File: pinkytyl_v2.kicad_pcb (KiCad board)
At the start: 2 copper layers, 132 x 105.9 mm, 66 parts, among them J1 50-00174, J2 Conn_01x02, J3 USB_B_Mini, J5 Conn_02x05_Odd_Even, K0 KEYSW, K10 KEYSW, K11 KEYSW, K12 KEYSW, K13 KEYSW, K14 KEYSW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

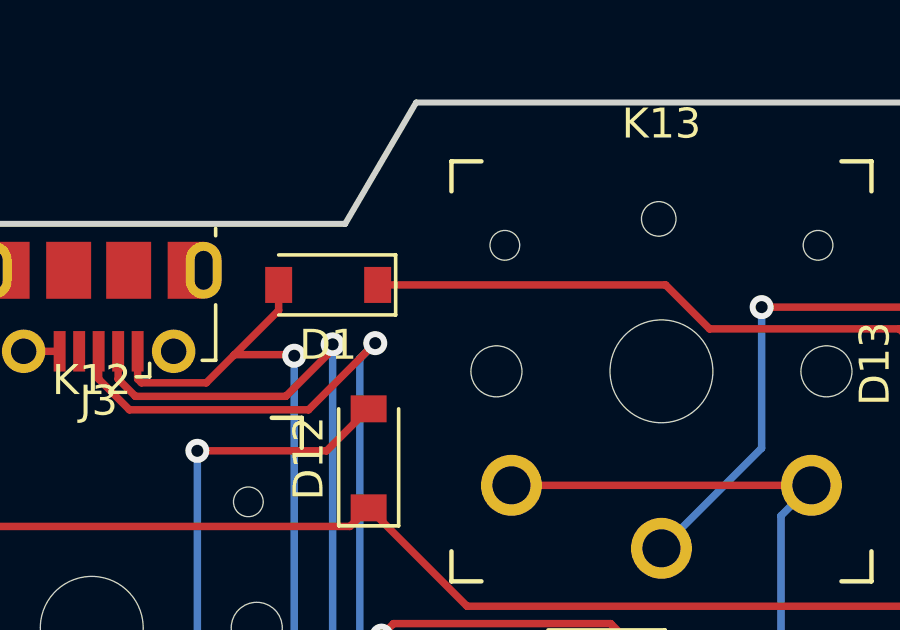
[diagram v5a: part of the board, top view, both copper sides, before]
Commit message: Changed my mind regarding detection of VUSB, software solution is doing fine with less components
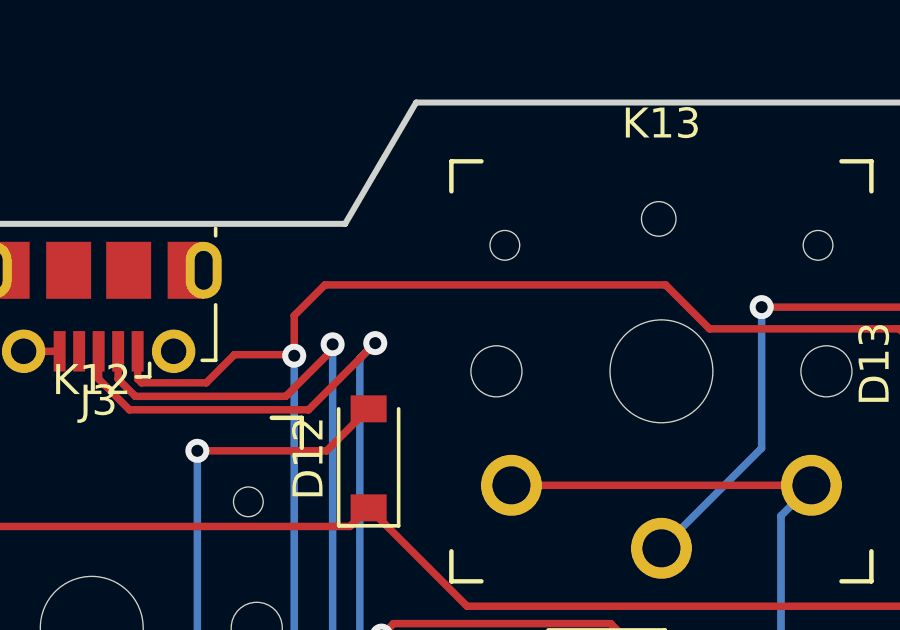
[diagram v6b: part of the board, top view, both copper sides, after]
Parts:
- removed D1: D, Diode_SMD:D_SOD-123
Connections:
- J3 pad 1: UVCC -> VCC
- U1 pad 7: UVCC -> VCC
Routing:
- net VCC: track 208.6 -> 326.3 mm, vias 7 -> 11
- net UVCC: track 116.1 -> 0.00 mm, vias 4 -> 0
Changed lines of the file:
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@@
     (tracks 594)
     (zones 0)
-    (modules 66)
-    (nets 64)
+    (modules 65)
+    (nets 63)
   )
   (page A4)
@@
   (net 61 "Net-(U1-Pad41)")
   (net 62 "Net-(D0-Pad2)")
-  (net 63 UVCC)
   (net_class Default "This is the default net class."
     (clearance 0.2)
@@
     (add_net "Net-(U1-Pad41)")
     (add_net "Net-(U1-Pad8)")
-    (add_net UVCC)
     (add_net VCC)
     (add_net c0)
@@
     (pad "" np_thru_hole circle (at -5.22 -4.2) (size 0.9906 0.9906) (drill 0.9906) (layers *.Cu *.Mask))
   )
-  (module Diode_SMD:D_SOD-123 (layer F.Cu)
-    (at 125.49 42.26 180)
-    (descr SOD-123)
-    (tags SOD-123)
-    (attr smd)
-    (fp_text reference D1 (at 0 -2) (layer F.SilkS)
-      (effects (font (size 1 1) (thickness 0.15)))
-    )
-    (fp_text value D (at 0 2.1) (layer F.Fab)
-      (effects (font (size 1 1) (thickness 0.15)))
-    )
-    (fp_text user %R (at 0 -2) (layer F.Fab)
-      (effects (font (size 1 1) (thickness 0.15)))
-    )
-    (fp_line (start -2.25 -1) (end -2.25 1) (layer F.SilkS) (width 0.12))
-    (fp_line (start 0.25 0) (end 0.75 0) (layer F.Fab) (width 0.1))
-    (fp_line (start 0.25 0.4) (end -0.35 0) (layer F.Fab) (width 0.1))
-    (fp_line (start 0.25 -0.4) (end 0.25 0.4) (layer F.Fab) (width 0.1))
-    (fp_line (start -0.35 0) (end 0.25 -0.4) (layer F.Fab) (width 0.1))
-    (fp_line (start -0.35 0) (end -0.35 0.55) (layer F.Fab) (width 0.1))
-    (fp_line (start -0.35 0) (end -0.35 -0.55) (layer F.Fab) (width 0.1))
-    (fp_line (start -0.75 0) (end -0.35 0) (layer F.Fab) (width 0.1))
-    (fp_line (start -1.4 0.9) (end -1.4 -0.9) (layer F.Fab) (width 0.1))
-    (fp_line (start 1.4 0.9) (end -1.4 0.9) (layer F.Fab) (width 0.1))
-    (fp_line (start 1.4 -0.9) (end 1.4 0.9) (layer F.Fab) (width 0.1))
-    (fp_line (start -1.4 -0.9) (end 1.4 -0.9) (layer F.Fab) (width 0.1))
-    (fp_line (start -2.35 -1.15) (end 2.35 -1.15) (layer F.CrtYd) (width 0.05))
-    (fp_line (start 2.35 -1.15) (end 2.35 1.15) (layer F.CrtYd) (width 0.05))
-    (fp_line (start 2.35 1.15) (end -2.35 1.15) (layer F.CrtYd) (width 0.05))
-    (fp_line (start -2.35 -1.15) (end -2.35 1.15) (layer F.CrtYd) (width 0.05))
-    (fp_line (start -2.25 1) (end 1.65 1) (layer F.SilkS) (width 0.12))
-    (fp_line (start -2.25 -1) (end 1.65 -1) (layer F.SilkS) (width 0.12))
-    (pad 2 smd rect (at 1.65 0 180) (size 0.9 1.2) (layers F.Cu F.Paste F.Mask)
-      (net 63 UVCC))
-    (pad 1 smd rect (at -1.65 0 180) (size 0.9 1.2) (layers F.Cu F.Paste F.Mask)
-      (net 1 VCC))
-    (model ${KISYS3DMOD}/Diode_SMD.3dshapes/D_SOD-123.wrl
-      (at (xyz 0 0 0))
-      (scale (xyz 1 1 1))
-      (rotate (xyz 0 0 0))
-    )
-  )
   (module Logos:JLCPCB_MountingHole_1.152mm locked (layer F.Cu)
     (at 136.51 40.06)
@@
       (net 48 "Net-(U1-Pad8)"))
     (pad 7 smd rect (at -5.7 0.8 180) (size 1.5 0.55) (layers F.Cu F.Paste F.Mask)
-      (net 63 UVCC))
+      (net 1 VCC))
     (pad 6 smd rect (at -5.7 0 180) (size 1.5 0.55) (layers F.Cu F.Paste F.Mask)
       (net 6 "Net-(C7-Pad1)"))
@@
       (net 32 d-))
     (pad 1 smd rect (at -1.3 -1.4625 180) (size 0.4 1.35) (layers F.Cu F.Paste F.Mask)
-      (net 63 UVCC))
+      (net 1 VCC))
     (pad 5 smd rect (at 1.3 -1.4625 180) (size 0.4 1.35) (layers F.Cu F.Paste F.Mask)
       (net 2 GND))
@@
   (segment (start 187.52 57.53) (end 178.6 48.61) (width 0.25) (layer B.Cu) (net 1))
   (segment (start 187.52 58.68) (end 187.52 57.53) (width 0.25) (layer B.Cu) (net 1))
-  (segment (start 136.738462 42.26) (end 127.14 42.26) (width 0.25) (layer F.Cu) (net 1))
-  (segment (start 144.530003 43.725001) (end 138.203463 43.725001) (width 0.25) (layer F.Cu) (net 1))
-  (segment (start 149.235002 48.43) (end 144.530003 43.725001) (width 0.25) (layer F.Cu) (net 1))
-  (segment (start 138.203463 43.725001) (end 136.738462 42.26) (width 0.25) (layer F.Cu) (net 1))
-  (segment (start 178.6 48.43) (end 149.235002 48.43) (width 0.25) (layer F.Cu) (net 1))
   (via (at 181.28 102.34) (size 0.8) (drill 0.4) (layers F.Cu B.Cu) (net 1))
   (segment (start 181.28 64.92) (end 181.28 102.34) (width 0.25) (layer B.Cu) (net 1))
@@
   (segment (start 107.31 58.64) (end 108.07 59.4) (width 0.25) (layer F.Cu) (net 62))
   (segment (start 102.26 58.64) (end 107.31 58.64) (width 0.25) (layer F.Cu) (net 62))
-  (segment (start 119.265001 45.522501) (end 121.427499 45.522501) (width 0.25) (layer F.Cu) (net 63))
-  (segment (start 119.14 45.3975) (end 119.265001 45.522501) (width 0.25) (layer F.Cu) (net 63))
-  (segment (start 123.84 43.11) (end 123.84 42.26) (width 0.25) (layer F.Cu) (net 63))
-  (segment (start 119.14 44.4725) (end 119.14 45.3975) (width 0.25) (layer F.Cu) (net 63))
-  (via (at 124.36 44.62) (size 0.8) (drill 0.4) (layers F.Cu B.Cu) (net 63))
-  (segment (start 124.325 44.585) (end 124.36 44.62) (width 0.25) (layer F.Cu) (net 63))
-  (segment (start 122.365 44.585) (end 124.325 44.585) (width 0.25) (layer F.Cu) (net 63))
-  (segment (start 121.427499 45.522501) (end 122.365 44.585) (width 0.25) (layer F.Cu) (net 63))
-  (segment (start 122.365 44.585) (end 123.84 43.11) (width 0.25) (layer F.Cu) (net 63))
-  (segment (start 124.36 62.02) (end 124.38 62.04) (width 0.25) (layer B.Cu) (net 63))
-  (via (at 124.38 62.04) (size 0.8) (drill 0.4) (layers F.Cu B.Cu) (net 63))
-  (segment (start 124.36 44.62) (end 124.36 62.02) (width 0.25) (layer B.Cu) (net 63))
-  (via (at 165.36 63.13) (size 0.8) (drill 0.4) (layers F.Cu B.Cu) (net 63))
-  (segment (start 149.94641 63.13) (end 165.36 63.13) (width 0.25) (layer F.Cu) (net 63))
-  (segment (start 148.456411 61.640001) (end 149.94641 63.13) (width 0.25) (layer F.Cu) (net 63))
-  (segment (start 124.779999 61.640001) (end 148.456411 61.640001) (width 0.25) (layer F.Cu) (net 63))
-  (segment (start 124.38 62.04) (end 124.779999 61.640001) (width 0.25) (layer F.Cu) (net 63))
-  (via (at 165.37 107.26) (size 0.8) (drill 0.4) (layers F.Cu B.Cu) (net 63))
-  (segment (start 165.36 107.25) (end 165.37 107.26) (width 0.25) (layer B.Cu) (net 63))
-  (segment (start 165.36 63.13) (end 165.36 107.25) (width 0.25) (layer B.Cu) (net 63))
-  (segment (start 168.61 107.26) (end 168.62 107.27) (width 0.25) (layer F.Cu) (net 63))
-  (segment (start 165.37 107.26) (end 168.61 107.26) (width 0.25) (layer F.Cu) (net 63))
+  (segment (start 119.265001 45.522501) (end 121.427499 45.522501) (width 0.25) (layer F.Cu) (net 1))
+  (segment (start 119.14 45.3975) (end 119.265001 45.522501) (width 0.25) (layer F.Cu) (net 1))
+  (segment (start 119.14 44.4725) (end 119.14 45.3975) (width 0.25) (layer F.Cu) (net 1))
+  (via (at 124.36 44.62) (size 0.8) (drill 0.4) (layers F.Cu B.Cu) (net 1))
+  (segment (start 124.325 44.585) (end 124.36 44.62) (width 0.25) (layer F.Cu) (net 1))
+  (segment (start 122.365 44.585) (end 124.325 44.585) (width 0.25) (layer F.Cu) (net 1))
+  (segment (start 121.427499 45.522501) (end 122.365 44.585) (width 0.25) (layer F.Cu) (net 1))
+  (segment (start 124.36 62.02) (end 124.38 62.04) (width 0.25) (layer B.Cu) (net 1))
+  (via (at 124.38 62.04) (size 0.8) (drill 0.4) (layers F.Cu B.Cu) (net 1))
+  (segment (start 124.36 44.62) (end 124.36 62.02) (width 0.25) (layer B.Cu) (net 1))
+  (via (at 165.36 63.13) (size 0.8) (drill 0.4) (layers F.Cu B.Cu) (net 1))
+  (segment (start 149.94641 63.13) (end 165.36 63.13) (width 0.25) (layer F.Cu) (net 1))
+  (segment (start 148.456411 61.640001) (end 149.94641 63.13) (width 0.25) (layer F.Cu) (net 1))
+  (segment (start 124.779999 61.640001) (end 148.456411 61.640001) (width 0.25) (layer F.Cu) (net 1))
+  (segment (start 124.38 62.04) (end 124.779999 61.640001) (width 0.25) (layer F.Cu) (net 1))
+  (via (at 165.37 107.26) (size 0.8) (drill 0.4) (layers F.Cu B.Cu) (net 1))
+  (segment (start 165.36 107.25) (end 165.37 107.26) (width 0.25) (layer B.Cu) (net 1))
+  (segment (start 165.36 63.13) (end 165.36 107.25) (width 0.25) (layer B.Cu) (net 1))
+  (segment (start 168.61 107.26) (end 168.62 107.27) (width 0.25) (layer F.Cu) (net 1))
+  (segment (start 165.37 107.26) (end 168.61 107.26) (width 0.25) (layer F.Cu) (net 1))
+  (segment (start 125.38 42.26) (end 124.36 43.28) (width 0.25) (layer F.Cu) (net 1))
+  (segment (start 136.738462 42.26) (end 125.38 42.26) (width 0.25) (layer F.Cu) (net 1))
+  (segment (start 138.203463 43.725001) (end 136.738462 42.26) (width 0.25) (layer F.Cu) (net 1))
+  (segment (start 144.530003 43.725001) (end 138.203463 43.725001) (width 0.25) (layer F.Cu) (net 1))
+  (segment (start 149.235002 48.43) (end 144.530003 43.725001) (width 0.25) (layer F.Cu) (net 1))
+  (segment (start 178.6 48.43) (end 149.235002 48.43) (width 0.25) (layer F.Cu) (net 1))
+  (segment (start 124.36 44.62) (end 124.36 43.28) (width 0.25) (layer F.Cu) (net 1))
   (zone (net 2) (net_name GND) (layer F.Cu) (hatch edge 0.508)
     (connect_pads (clearance 0.508))
